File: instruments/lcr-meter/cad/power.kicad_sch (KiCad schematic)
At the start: 48 parts, among them J2 5V 1A CENTER+, Q1 AO3401A, U11 TPS7A4901DGNR, U12 TPS7A3001DGNR, U13 TPS65131RGER, U3 3.3V AP2112K

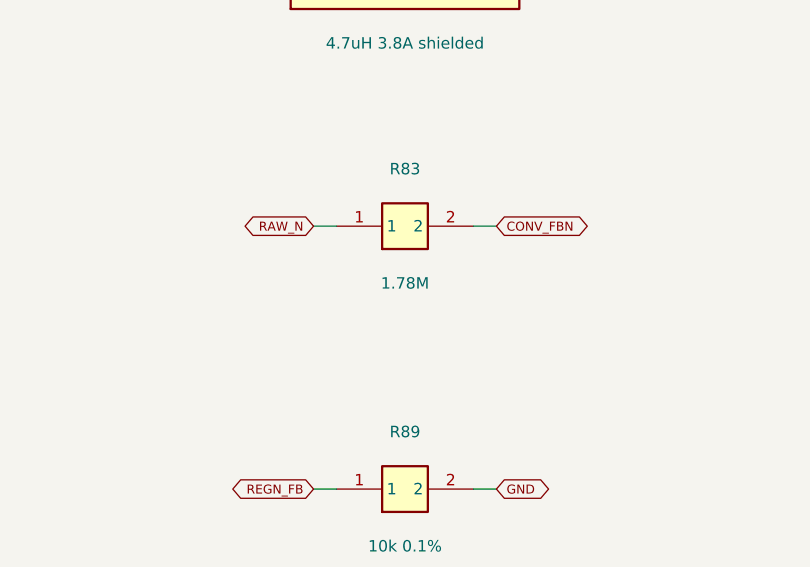
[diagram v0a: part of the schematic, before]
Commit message: lcr-meter Rev D: R94 22 ohm LO isolation, R83 1.74M
- R94 (RT0603BRD0722RL, 22R 0.1% 25ppm) at (167.0,105.3) between J3 LO
  (DUT_LO) and the new TIA_SUM net (U7.2, C104.1, R43-R45.1). The LOW
  follower (U7.5) keeps the J3 F.Cu route, so channel A is the DUT voltage.
  J3.2 reaches R94.1 by a new B.Cu branch and via; the U7 under-body link
  now rises to R94.2; new In1/In2/B keepout under R94.2. Hand-routed per
  validation/layout-parasitics (placement shifted up 0.1 mm for courtyard).
- R83 1.78M -> 1.74M (0603WAF1744T5E) per validation/power-spurs R6.
- AFE schematic page draws R94 with the LOW tap on the J3 side; title
  blocks and silk say Rev D; U7 reference moved clear of R94.
- Adds cad/tools/dump_copper.py + region_view.py for hand-routing views.

rebuild.sh: ERC 0, DRC 0, 0 unconnected, schematic parity 0, DFM audit pass.
LCSC stock for the new lines is to be confirmed at JLC BOM upload.

Co-Authored-By: Claude Opus 5.5 <noreply@anthropic.com>
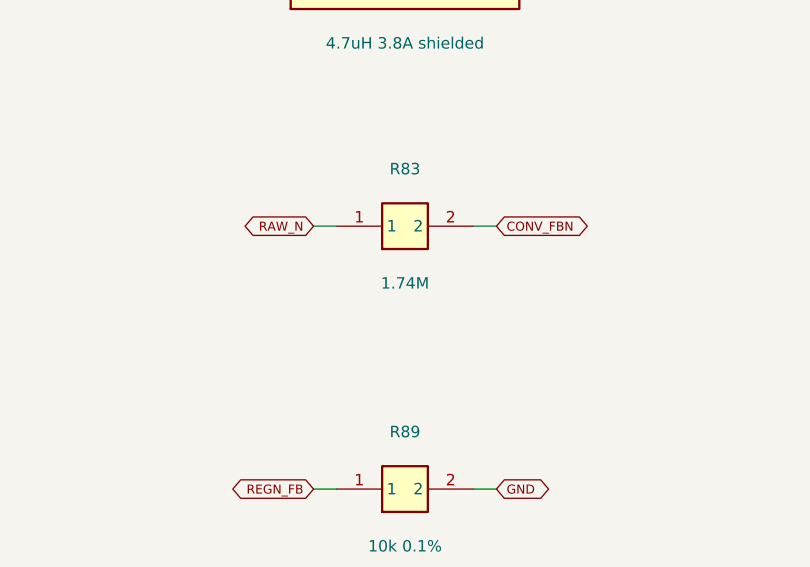
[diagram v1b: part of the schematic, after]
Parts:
- R83: value 1.78M -> 1.74M; LCSC C482655 -> C422975; MPN RC0603FR-071M78L -> 0603WAF1744T5E; Manufacturer YAGEO -> UNI-ROYAL(Uniroyal Elec); Unit_USD 0.0019 -> 0.0013

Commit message: lcr-meter Rev D: 1 ohm series resistors ahead of both LDO inputs
R95 (RAW_P -> LDOIN_P, at 109.6,141.77) and R96 (RAW_N -> LDOIN_N, at
98.6,136.0 rot 270) put a 1 ohm element between the TPS65131 outputs and
each LDO input, with C94/C97 and C99/C102 on the LDO side, per
validation/power-spurs R5 (switcher error on the +/-12 V path x17 lower;
headroom >= 1.26 V at 2x load). RAW_N now leaves the converter hub via on
F.Cu through R96 and drops to In2 at a new via (98.6,138.0). LDOIN_P/N get
power flags. Part 0603WAF100KT5E (C22936, basic).

rebuild.sh: ERC 0, DRC 0, 0 unconnected, parity 0.

Co-Authored-By: Claude Opus 5.5 <noreply@anthropic.com>
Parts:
- added R95, R96: 1R, LCR:R_0603_1608Metric, symbol LCR:R
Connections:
- net RAW_N: now also R96.1; no longer C102.1, C99.1, U12.5 (EN), U12.8 (IN)
- net RAW_P: now also R95.1; no longer C94.1, C97.1, U11.5 (EN), U11.8 (IN)
- new net LDOIN_N: C102.1, C99.1, R96.2, U12.5 (EN), U12.8 (IN)
- new net LDOIN_P: C94.1, C97.1, R95.2, U11.5 (EN), U11.8 (IN)
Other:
- moved on the sheet: C100, C101, C102, C103, C16, C17, C18, C80, C81, C82, C83, C84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

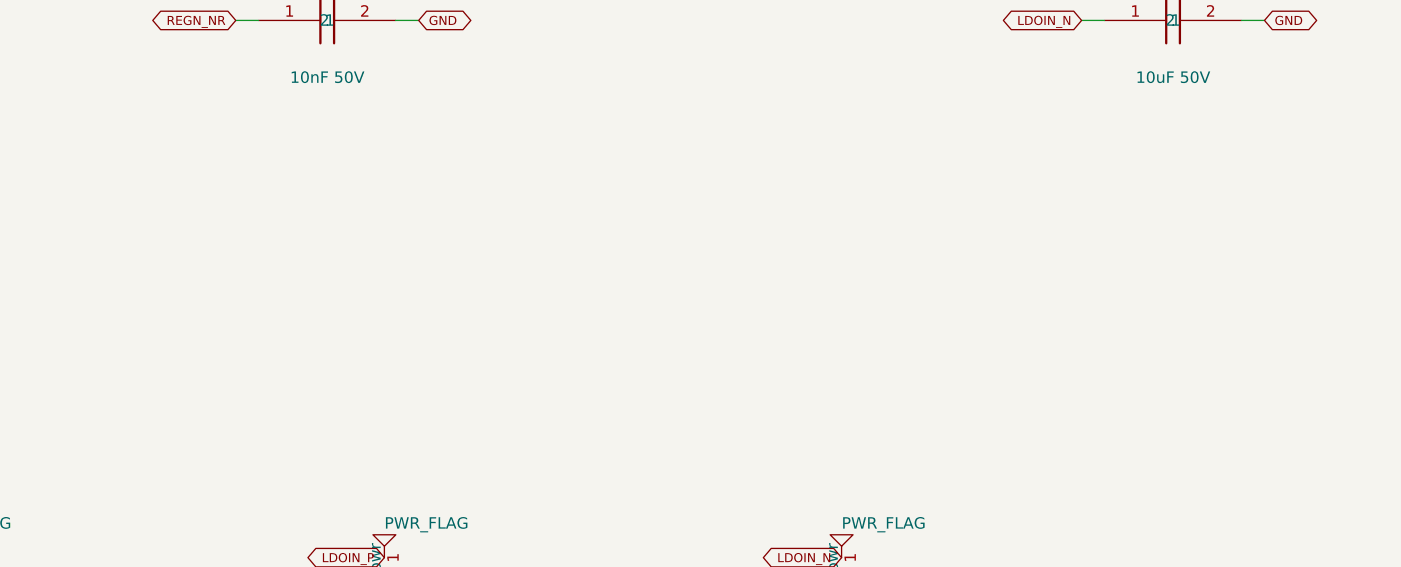
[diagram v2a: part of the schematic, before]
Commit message: lcr-meter Rev D: +12 V / -12 V rail monitors on RP2040 ADC0/ADC1
- MON12 (GPIO26, U1.38): R97 100k from 12V (tapped by a via on the In2 12V
  trunk at 109.01,112.6) to R98 10k + C110 100nF to GND at U1: ~1.09 V at
  12 V.
- MON_N12 (GPIO27, U1.39): R100 150k from -12V (T onto the F.Cu -12V trunk
  at x 124.95) to R99 10k to 3V3 + C111 100nF at U1: ~2.3 V at -12 V,
  3.1 V if the rail is absent, never negative while 3V3 is up.
- Divider top resistors sit at the rail ends, so the long B.Cu runs carry
  only a 100k/150k-limited node; filter caps sit at the ADC pins. MON12
  passes west of the 3V3 via; MON_N12 hops the B.Cu 3V3 trunk on In2.
  Reuses existing BOM lines only (C25803, C25804, C22807, C14663).

rebuild.sh: ERC 0, DRC 0, 0 unconnected, parity 0.

Co-Authored-By: Claude Opus 5.5 <noreply@anthropic.com>
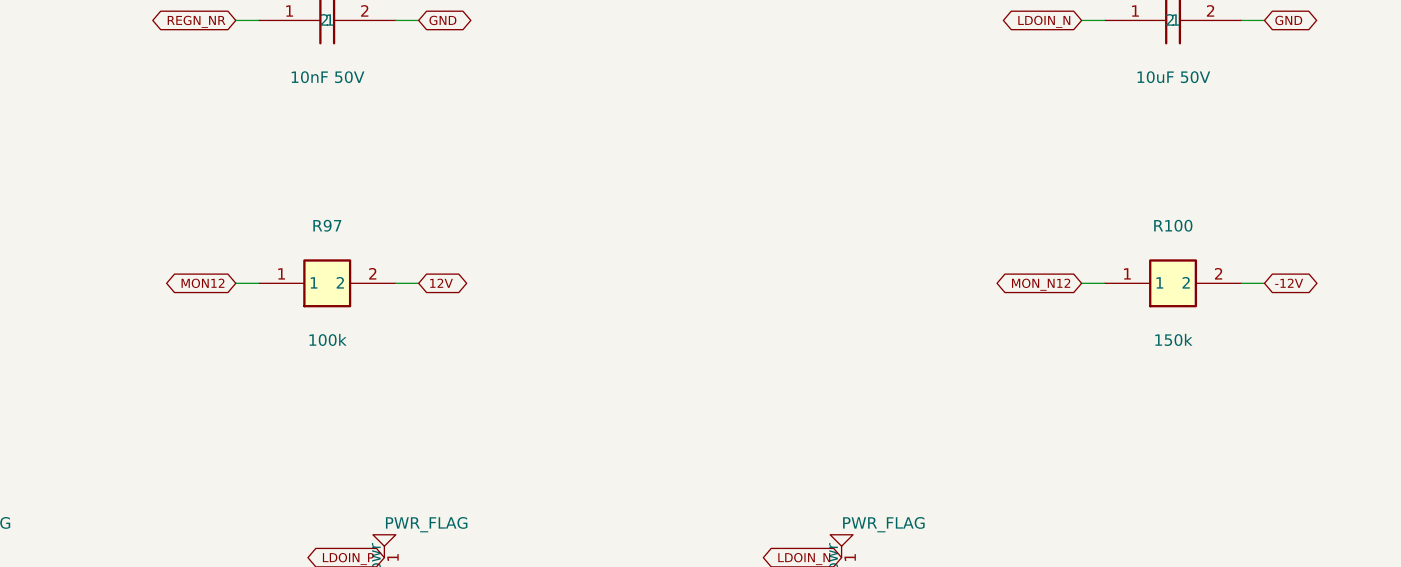
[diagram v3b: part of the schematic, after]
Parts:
- added R100: 150k, LCR:R_0603_1608Metric, symbol LCR:R
- added R97: 100k, LCR:R_0603_1608Metric, symbol LCR:R
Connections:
- net -12V: now also R100.2
- net 12V: now also R97.2
- new net MON12: R97.1
- new net MON_N12: R100.1

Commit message: lcr-meter Rev D: apply Tier 1 audit fixes
Hand-routed layout edits (cad/tools/edit_lib.py, no autorouter):
- Vias in every exposed pad: U1 8, U8/U9/U10 5, U11/U12 6 (were 0), U13 9.
- ADS9224R: 10 uF X7R 0805 reference caps at 1.56 mm, REFM joined to the
  cap before its via; 1 uF AVDD caps at 1.67/2.46 mm from pins 12/29.
- TPS7A4901/TPS7A3001: support parts packed per TI layout; FB nodes
  13.2/12.0 -> 5.2/5.3 mm, NR 2.1 mm. LDOIN_N In2 run moved off the pads.
- TPS65131 dividers compacted: CONV_FBP 13.1 -> 9.1 mm, CONV_FBN 16.8 -> 12.3 mm.
- RP2040: 1 uF at VREG_VIN (C5).

Parts: red status LED, basic ferrites, W25Q128JV flash (stock), C84,
CL32B106KBJNNNE on the 14 V and converter-input caps, C18/C103 basic,
C36 1 uF -> 100 nF. Extended lines 34 -> 30.

Firmware: settle max(150 ms, 20 cycles); BOOT -> reset_usb_boot().
Host 0.7.0: `temper-lcr boot PORT`.

Withdrawn after checking: converter dividers to TI example values (VPOS
15.105 V at the tolerance stack), 1 % LDO dividers (U12 headroom 0.74 V),
SRV05-4 (pinout unverifiable). regulator_check.py now reads design.json
instead of stale Rev C values.

DRC 0, unconnected 0, parity 0, ERC 0; independent check 576 pins, 0
findings; host 29 tests pass.

Co-Authored-By: Claude Opus 5.5 <noreply@anthropic.com>
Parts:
- C100, C80, C82, C89, C90, C91, C92, C94, C95, C99: value 10uF 50V -> 10uF 50V X7R; LCSC C337485 -> C138687; MPN UMK325AB7106KM-P -> CL32B106KBJNNNE; Manufacturer Taiyo Yuden -> Samsung Electro-Mechanics; Unit_USD 0.3394 -> 0.33
- C103: value 22uF 25V -> 22uF 25V X5R; footprint LCR:C_1210_3225Metric -> LCR:C_1206_3216Metric; LCSC C21397 -> C12891; MPN GRM32ER71E226KE15L -> CL31A226KAHNNNE; Manufacturer Murata Electronics -> Samsung Electro-Mechanics; Unit_USD 0.4151 -> 0.1798
- C18: value 10uF 50V -> 10uF 25V X5R; footprint LCR:C_1210_3225Metric -> LCR:C_0805_2012Metric; LCSC C337485 -> C15850; MPN UMK325AB7106KM-P -> CL21A106KAYNNNE; Manufacturer Taiyo Yuden -> Samsung Electro-Mechanics; Unit_USD 0.3394 -> 0.0773
- C84: value 220nF 50V -> 220nF 25V; LCSC C107083 -> C21120; MPN CC0603KRX7R9BB224 -> CL10B224KA8NNNC; Manufacturer YAGEO -> Samsung Electro-Mechanics; Unit_USD 0.0152 -> 0.0097
- FB1: value 120R@100MHz 3A -> 100R@100MHz 800mA; LCSC C79382 -> C1015; MPN BLM21PG121SN1D -> GZ2012D101TF; Manufacturer Murata Electronics -> Sunlord; Unit_USD 0.0406 -> 0.0311

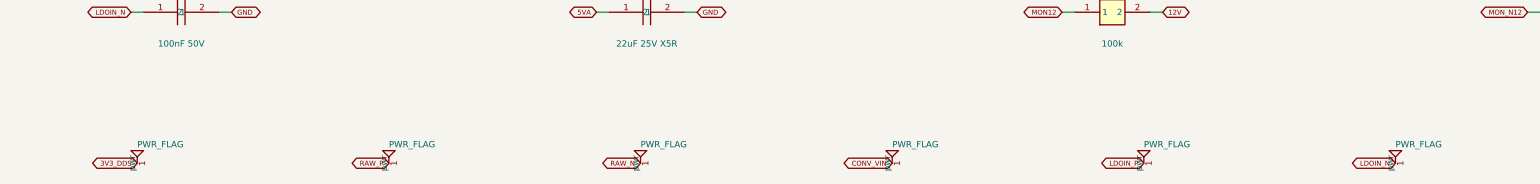
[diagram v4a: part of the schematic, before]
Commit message: feat(lcr): Rev E board with TAC5112 codec front end and relay ranges
Hand-routed Rev E on the Rev D outline:
- removes the ADS9224R, AD9833, both THS4551s, FB2 and JP1-JP6;
- adds the TAC5112 with its own AP2112K for 3V3A, three TQ2SA latching
  relays and their AO3400A drivers.

cad/tools/rev_e.py builds design.json and routing.json from the Rev D
package. rev_e_routes.py gives every new segment and via by coordinate.

Details:
- Every via is now a 0.3 mm drill with a pad of 0.45 mm or more.
  The board rules set a 0.30 mm minimum hole and a 0.075 mm minimum
  annular ring.
- Basic-library swaps: D1 is now SRV05-4, and SW1/SW2 are now TS-1088.
- placement_offsets.py adds JLC CPL offsets for the new keyed parts,
  read from the lceda.cn EasyEDA mirror (easyeda.com returns 403). It
  reproduces the audited offsets for U3 (270) and Q1 (180).

Checks:
- rebuild.sh: ERC 0, DRC 0 violations and 0 unconnected, parity 0.
- package_cad and audit_dfm pass: 34 intended via-in-pad, none
  unexpected.
- independent_check.py e: 575 pins, 0 findings.

Co-Authored-By: Claude Opus 5.5 <noreply@anthropic.com>
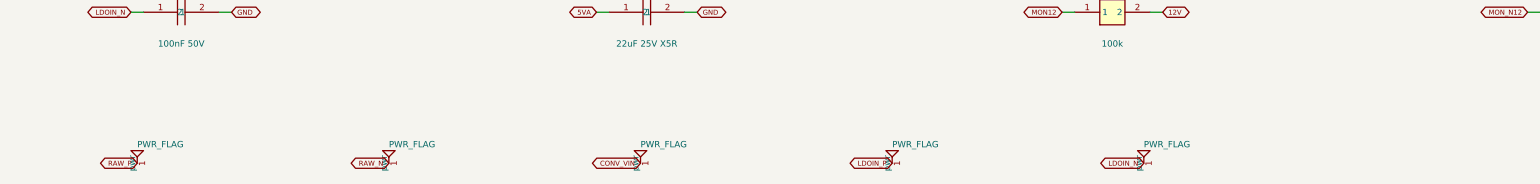
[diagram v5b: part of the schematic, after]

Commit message: lcr-meter: Rev E runs from USB-C power; DC jack and Q1 removed
U16 TPS2553 switches USB_VBUS onto 5V with built-in soft start and a
1.0-1.16 A current limit (R110 24k, SLVS841F eq. 1); EN tied to IN,
C113 1 uF at IN. VBUS runs hand-routed down the freed west strip; OUT
crosses the J5 3V3 feed on B.Cu into C80. ERC 0, DRC 0/0/0, independent
audit 624 pins 0 findings.

regulator_check: USB corners 4.40-5.5 V (4.32 V after U16), still 44/45.
rev_e_spurs: new mechanism 5, the coherent VBUS line needed for 1e-4
(>= 25 mV, 9 uF at 60.5 kHz). Five boards $453.46 -> $458.02.
archive_package hashes the tracked tree and names the Rev E package.

Co-Authored-By: Claude Opus 5.5 <noreply@anthropic.com>
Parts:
- removed J2: 5V 1A CENTER+, LCR:BarrelJack_Horizontal, symbol LCR:JACK
- removed Q1: AO3401A, LCR:SOT-23, symbol LCR:PMOS
- added C113: 1uF 50V, LCR:C_0805_2012Metric, symbol LCR:C
- added R110: 24k 1%, LCR:R_0603_1608Metric, symbol LCR:R
- added U16: TPS2553, LCR:SOT-23-6, symbol LCR:USBSW
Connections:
- net 5V: now also U16.6 (OUT)
- net GND: now also C113.2, R110.2, U16.2 (GND)
- new net USB_VBUS: C113.1, U16.1 (IN), U16.3 (EN)
- new net VBUS_ILIM: R110.1, U16.5 (ILIM)
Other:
- moved on the sheet: C100, C101, C102, C103, C16, C17, C18, C80, C81, C82, C83, C84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

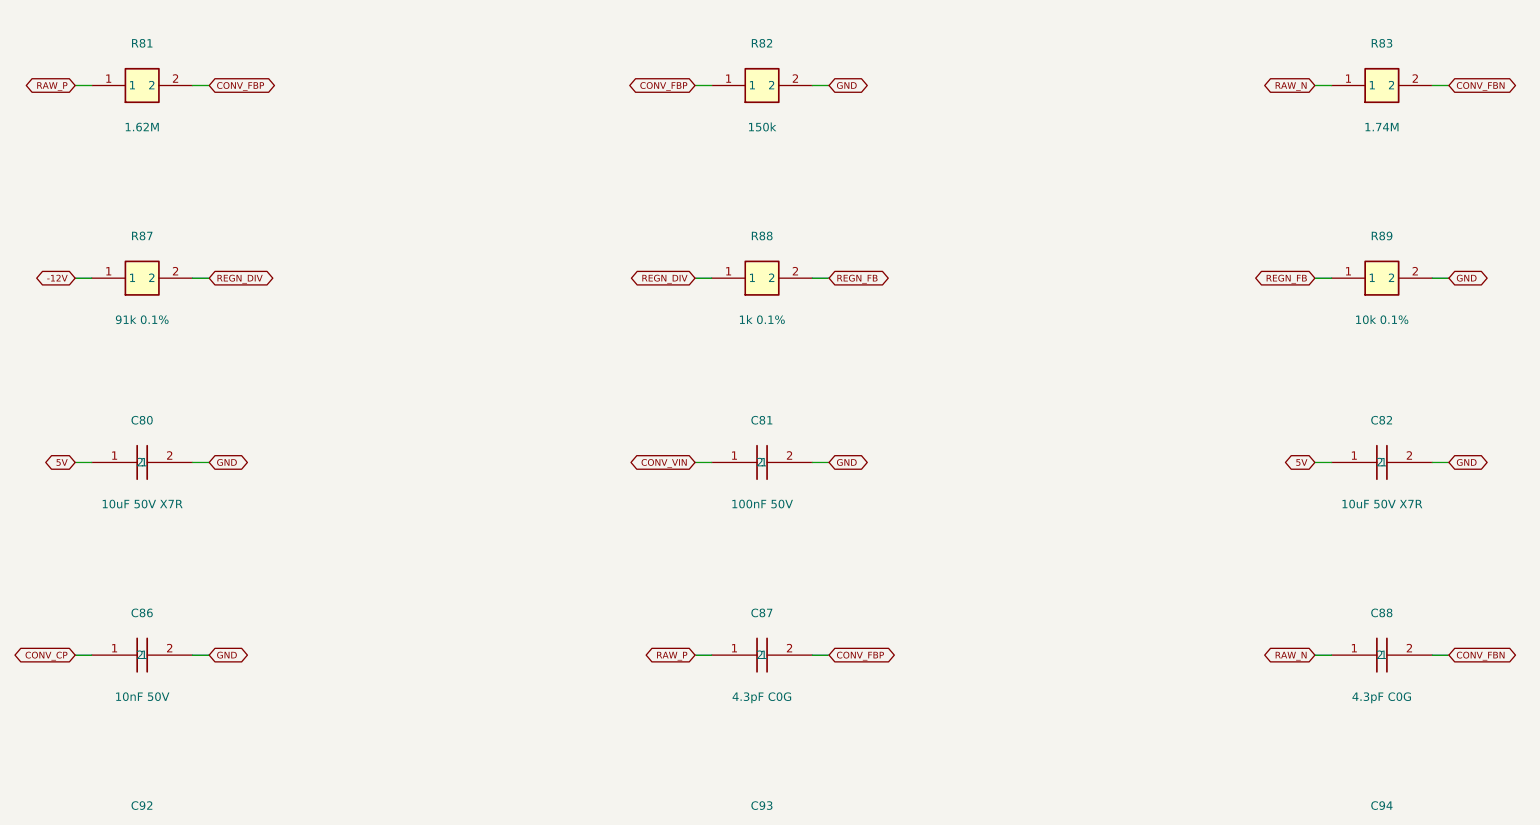
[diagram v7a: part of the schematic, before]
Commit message: lcr-meter: Rev E cost pass: tented vias (no POFV), two extended lines freed, 2k/5k 0.1 % restocked at 25 ppm
Five vias moved off small SMT lands (R3.2, C44.1, R101.1, U16.2, Y1.4); the 33
exposed-pad thermal vias stay, tented on B.Mask. audit_dfm.py now fails on a via
ring touching a land and on any untented via. Boost divider 430k/40.2k with 15 pF
and 4.7 pF feed-forward (preferred/basic). R32/R33 and R41/R44 move to Viking
25 ppm/C thin film (C728588 down to 22 in stock; the 5k was 50 ppm/C against the
budget). ERC 0, DRC 0/0/0, independent check 0, layout audit unchanged.
Five boards: $458.02 -> $428.40.

Co-Authored-By: Claude Opus 5.5 <noreply@anthropic.com>
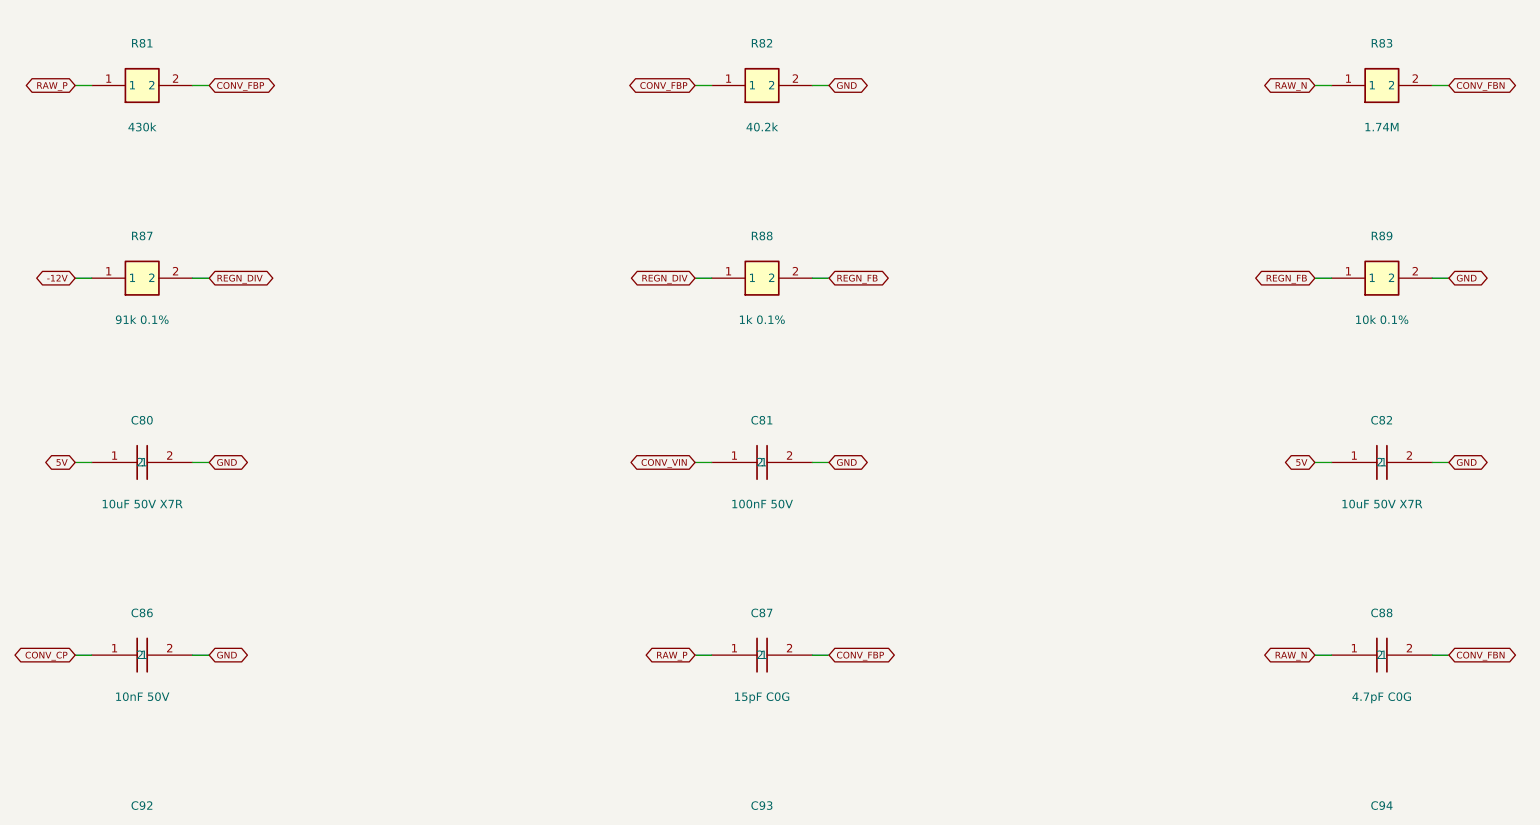
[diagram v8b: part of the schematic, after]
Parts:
- C87: value 4.3pF C0G -> 15pF C0G; LCSC C519375 -> C1644; MPN CC0603CRNPO9BN4R3 -> CL10C150JB8NNNC; Manufacturer YAGEO -> Samsung Electro-Mechanics; Unit_USD 0.0072 -> 0.0111
- C88: value 4.3pF C0G -> 4.7pF C0G; LCSC C519375 -> C1669; MPN CC0603CRNPO9BN4R3 -> 0603CG4R7C500NT; Manufacturer YAGEO -> FH (Guangdong Fenghua Advanced Tech); Unit_USD 0.0072 -> 0.0054
- R81: value 1.62M -> 430k; LCSC C482643 -> C25969; MPN RC0603FR-071M62L -> 0603WAF4303T5E; Manufacturer YAGEO -> UNI-ROYAL(Uniroyal Elec); Unit_USD 0.0018 -> 0.0031
- R82: value 150k -> 40.2k; LCSC C22807 -> C12447; MPN 0603WAF1503T5E -> 0603WAF4022T5E; Unit_USD 0.0017 -> 0.0021
